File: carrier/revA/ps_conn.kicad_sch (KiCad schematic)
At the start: 2 parts, among them J18 ICD26S13E6GV00LF, J8 0836149012

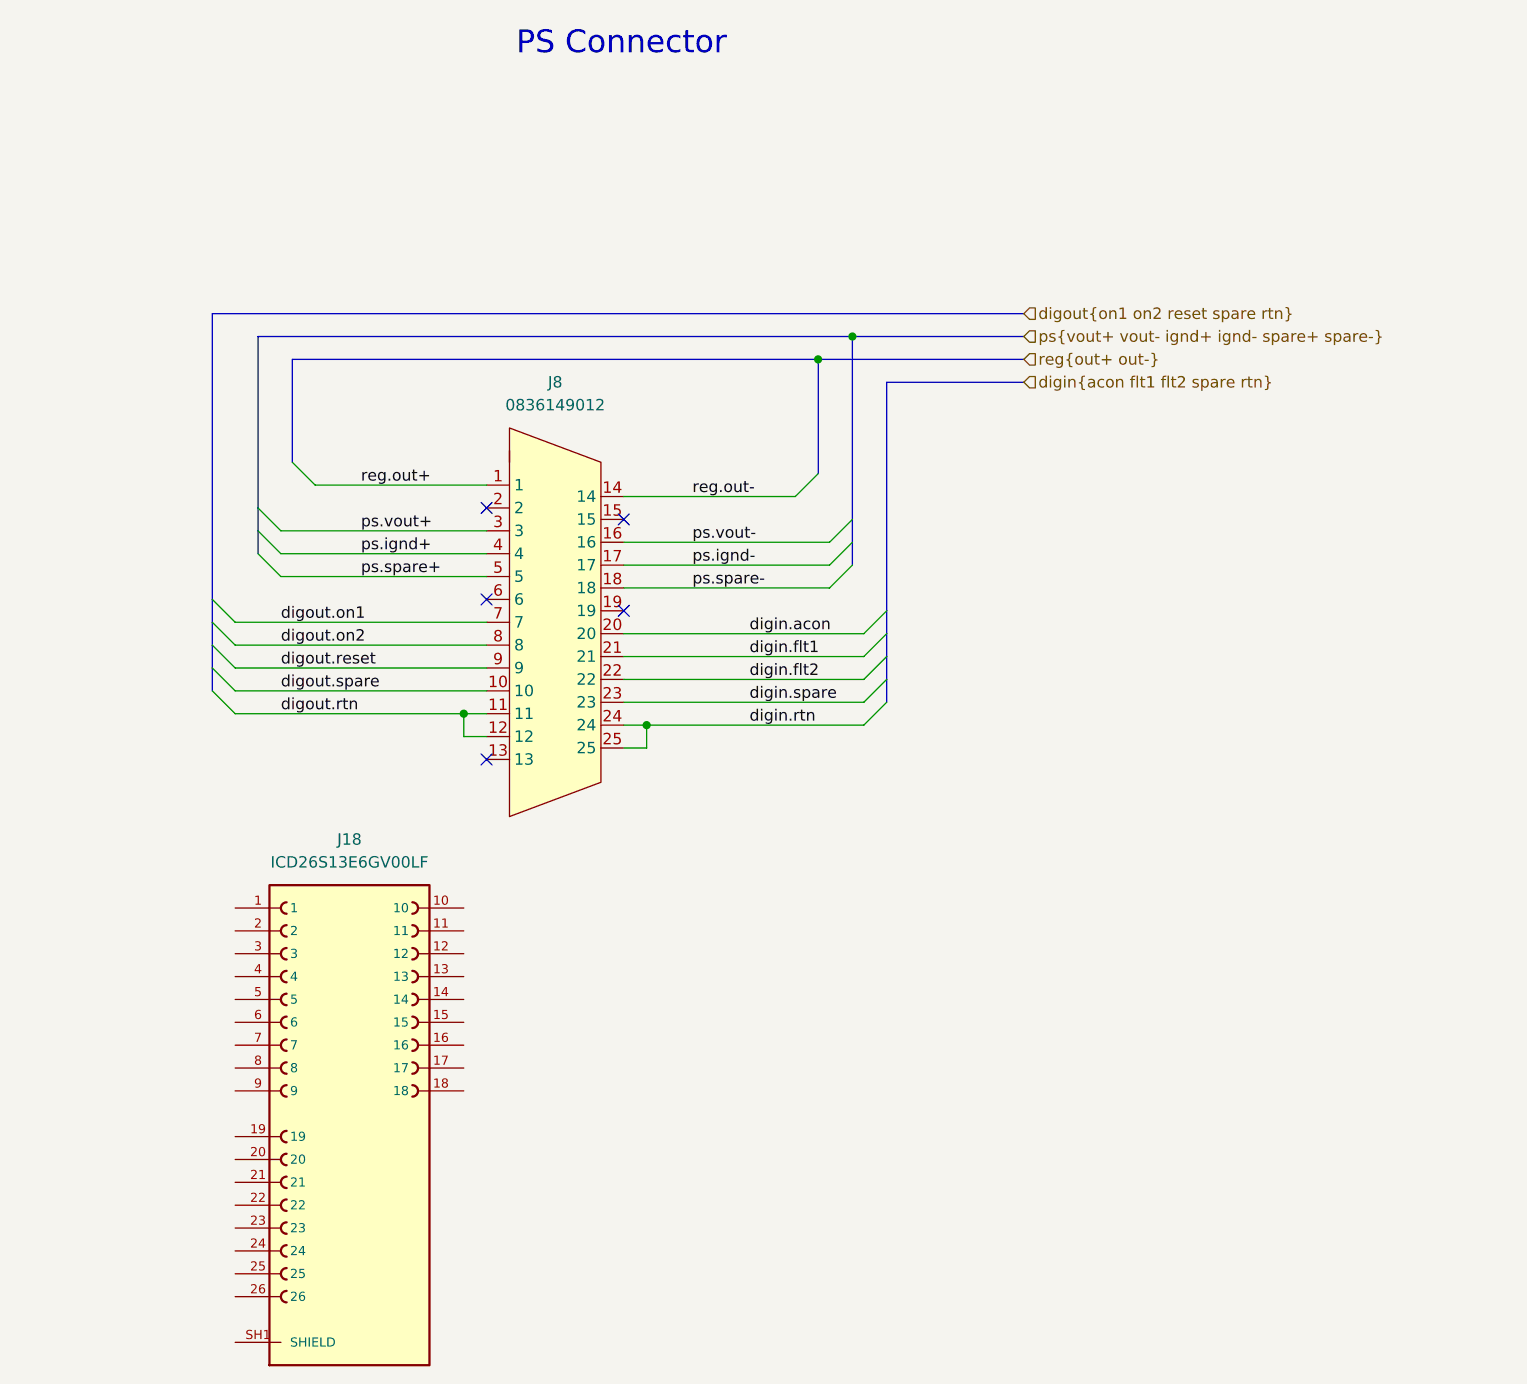
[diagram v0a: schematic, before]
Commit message: Add Edmundo PS connectors
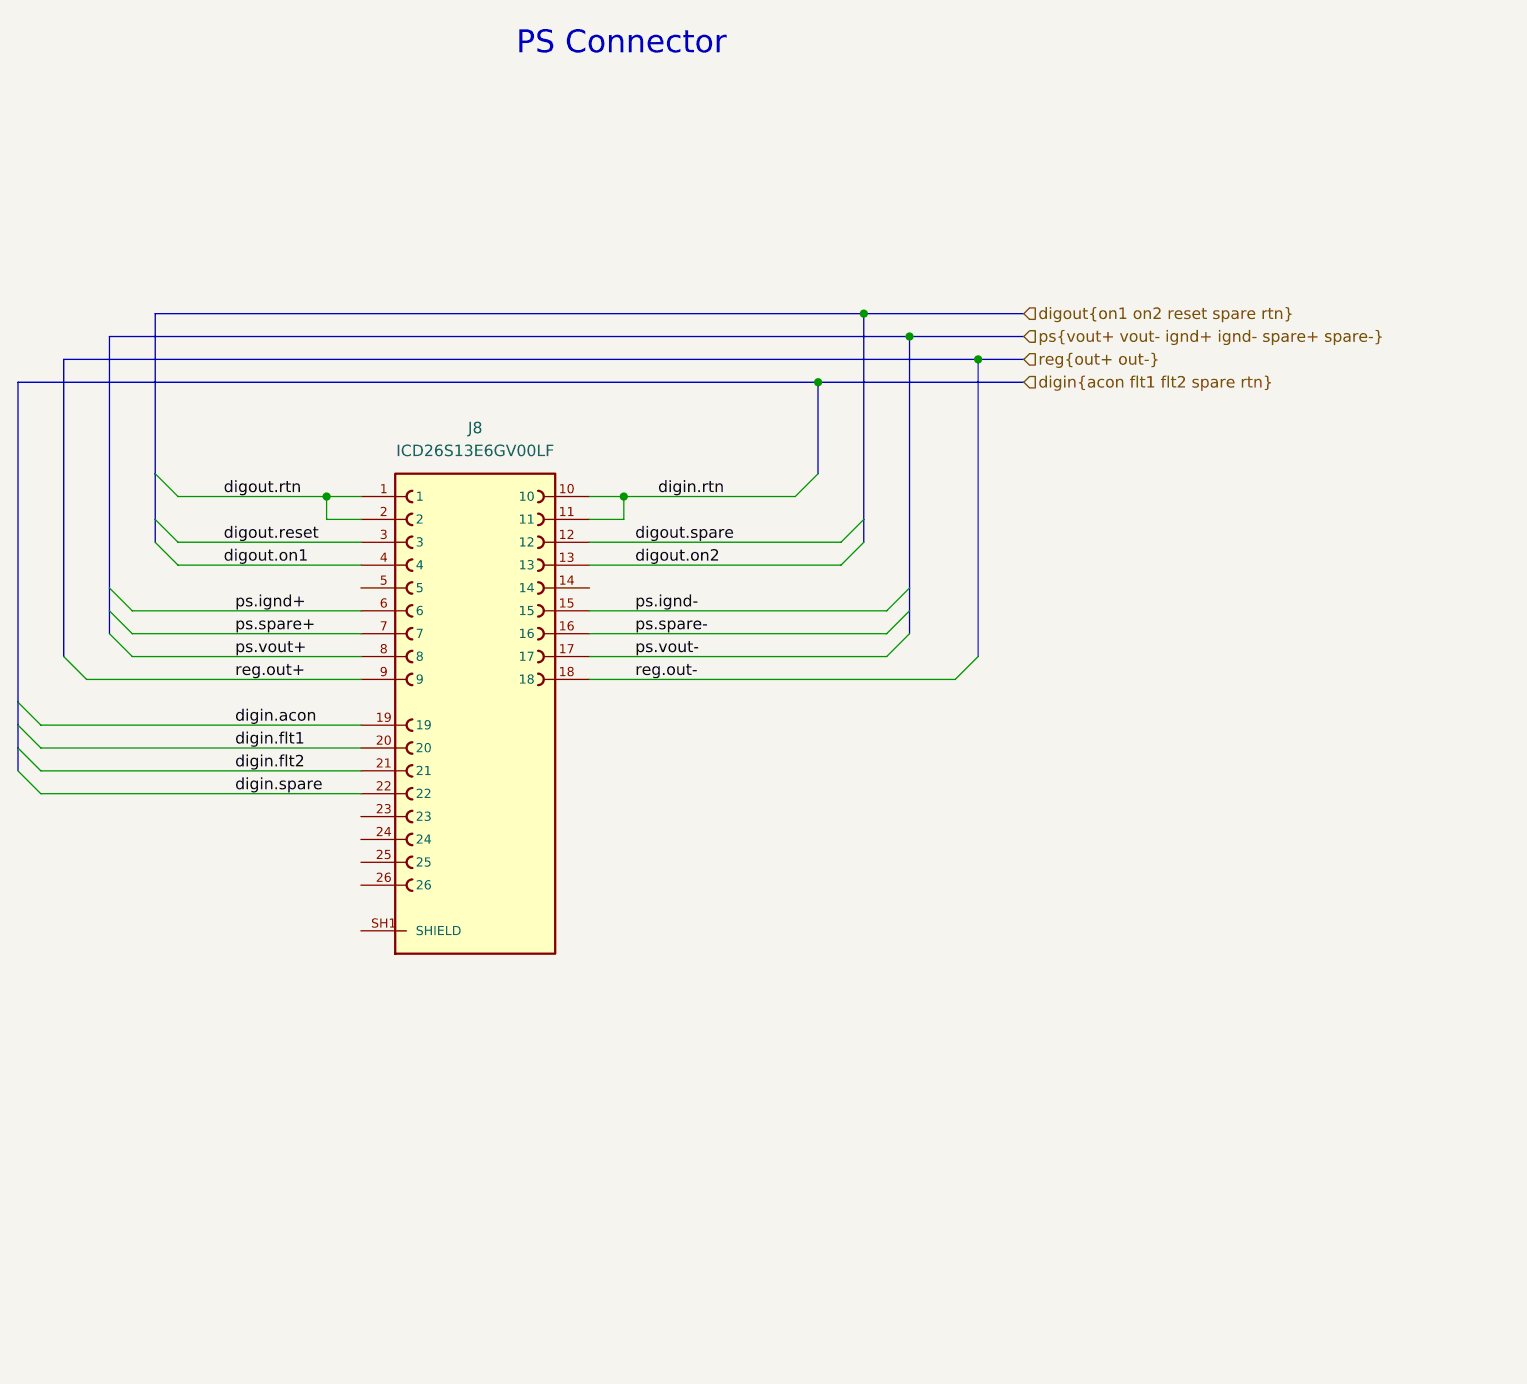
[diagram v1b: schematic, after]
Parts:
- removed J8: 0836149012, myparts:0836149012, symbol 0836149012:0836149012
- renumbered J18 to J8
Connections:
- net digin.acon: now also J8.19
- net digin.flt1: now also J8.20
- net digin.flt2: now also J8.21
- net digin.rtn: now also J8.10, J8.11
- net digin.spare: now also J8.22
- net digout.on1: now also J8.4
- net digout.on2: now also J8.13
- net digout.reset: now also J8.3
- net digout.rtn: now also J8.1, J8.2
- net digout.spare: now also J8.12
- net ps.ignd+: now also J8.6
- net ps.ignd-: now also J8.15
- net ps.spare+: now also J8.7
- net ps.spare-: now also J8.16
- net ps.vout+: now also J8.8
- net ps.vout-: now also J8.17
- net reg.out+: now also J8.9
- net reg.out-: now also J8.18
- no-connect marks 5 -> 0
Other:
- moved on the sheet: J8
